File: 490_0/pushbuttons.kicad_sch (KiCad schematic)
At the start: 5 parts, among them SW1 SW_Push0, SW2 SW_Push1, SW3 SW_Push2, SW4 SW_Push3, SW5 SW_Push4

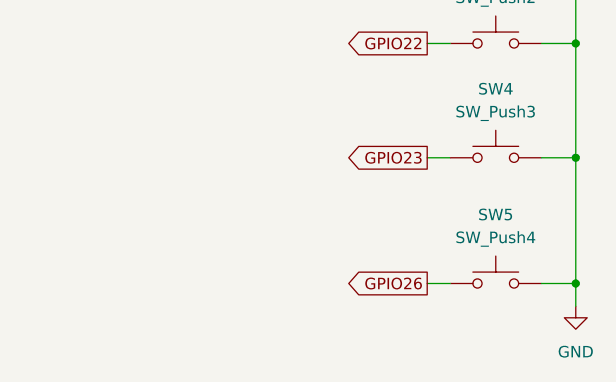
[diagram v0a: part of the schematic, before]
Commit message: US letter format
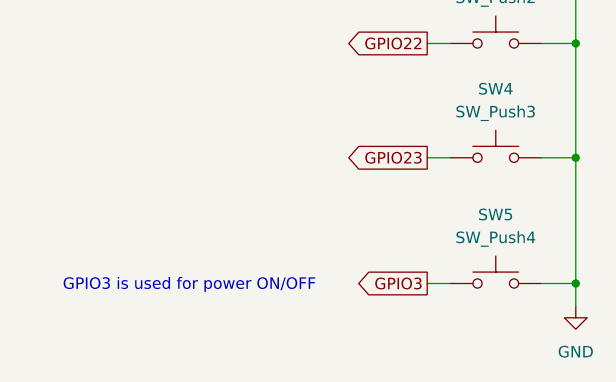
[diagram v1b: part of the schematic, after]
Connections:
- net GPIO26 renamed GPIO3
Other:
- note added: "GPIO3 is used for power ON/OFF"
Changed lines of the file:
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@@
 	(generator "eeschema")
 	(generator_version "9.0")
-	(paper "A4")
+	(paper "USLetter")
+	(text "GPIO3 is used for power ON/OFF\n"
+		(exclude_from_sim no)
+		(at 109.474 114.554 0)
+		(effects
+			(font
+				(size 1.27 1.27)
+			)
+		)
+	)
 	(junction
 		(at 152.4 100.33)
@@
 		)
 	)
-	(global_label "GPIO26"
+	(global_label "GPIO3"
 		(shape output)
 		(at 135.89 114.3 180)
@@
 		)
 		(property "Intersheetrefs" "${INTERSHEET_REFS}"
-			(at 126.0105 114.3 0)
+			(at 127.22 114.3 0)
 			(effects
 				(font

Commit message: Fixed buttons
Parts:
- removed SW1: SW_Push0, symbol Switch:SW_Push
- removed SW2: SW_Push1, symbol Switch:SW_Push
- removed SW3: SW_Push2, symbol Switch:SW_Push
- removed SW4: SW_Push3, symbol Switch:SW_Push
- removed SW5: SW_Push4, symbol Switch:SW_Push
- added R3, R4, R5, R6: 10k, symbol Device:R
- added SW10, SW11, SW12, SW6, SW7: SW_Push0, symbol Switch:SW_Push
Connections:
- net GND: now also SW10.1, SW11.1, SW12.1, SW6.1, SW7.1
- net GPIO16: now also R3.1, SW6.2
- net GPIO17: now also R4.1, SW7.2
- net GPIO22: now also R5.1, SW10.2
- net GPIO23: now also R6.1, SW11.2
- new net +3.3V: R3.2, R4.2, R5.2, R6.2, SW12.2
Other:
- note added: "CM4 has built in internal 1.8kΩ pull up to GPIO_VREF on GPIO3"
- note added: "To Turn ON: When the Pi is OFF/halted - shorting GPIO3 to Ground wakes it up. To Turn OFF: When the Pi is ON - run a script that listens for a button press on GPIO3 and issues the command sudo shutdown -h now"
- note removed: "GPIO3 is used for power ON/OFF"

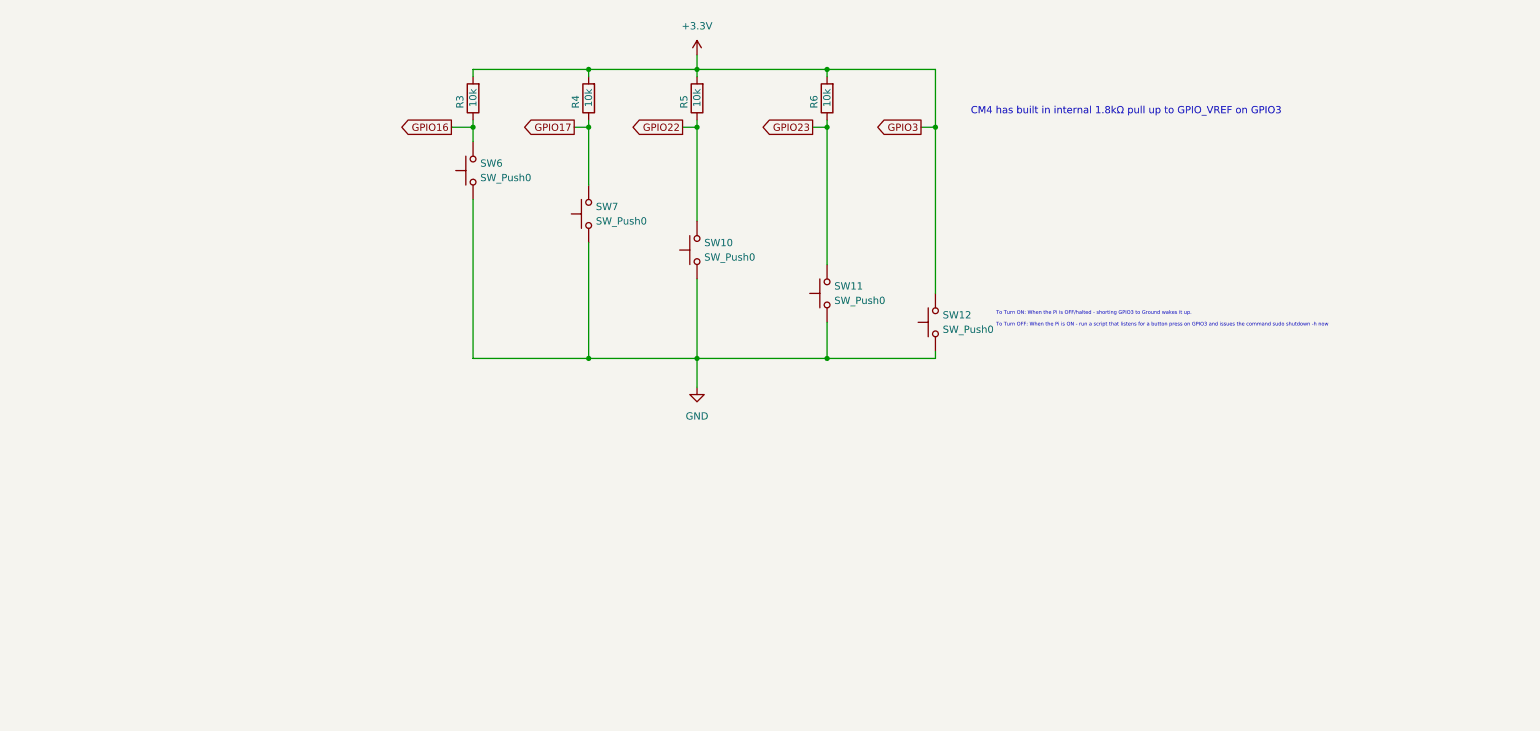
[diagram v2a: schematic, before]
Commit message: Added debouncing to the buttons
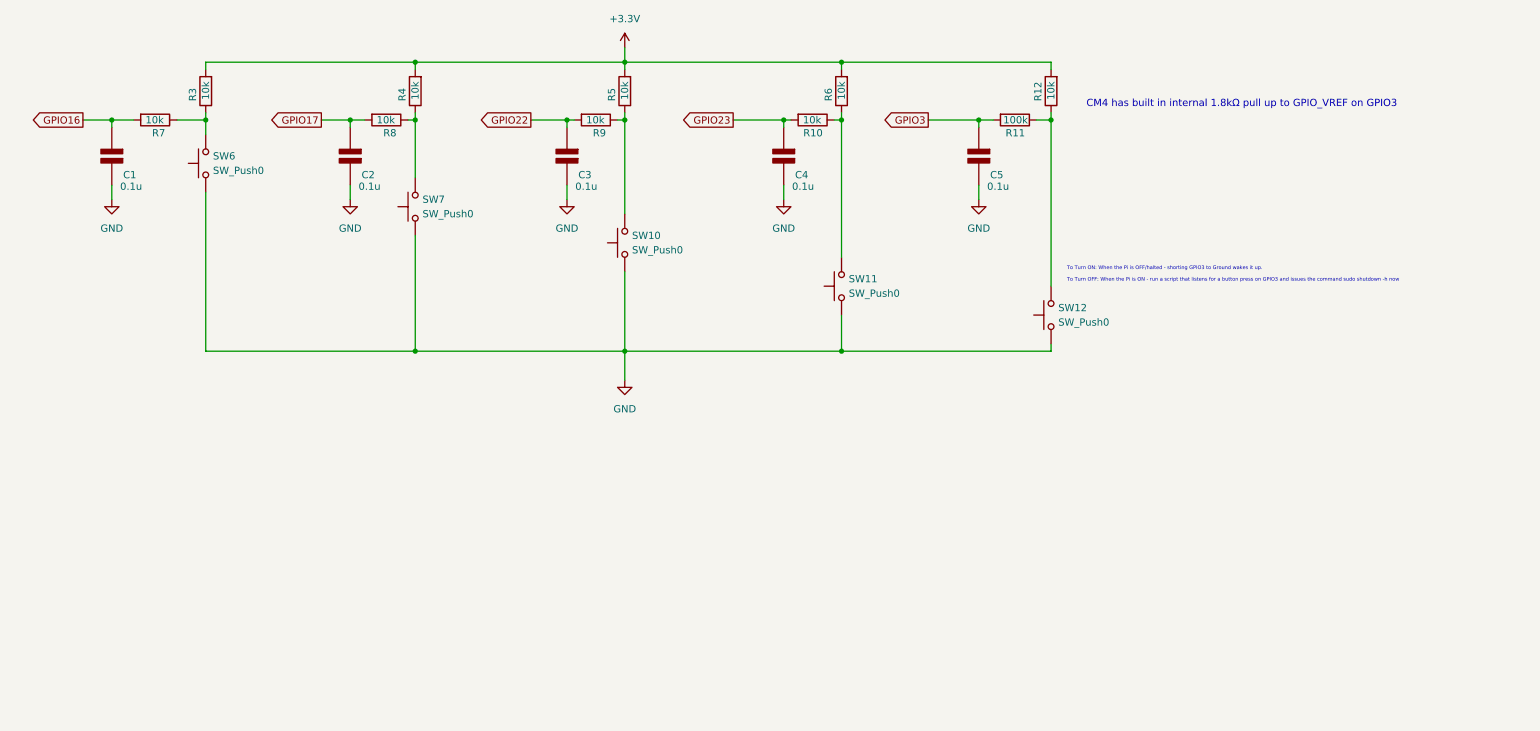
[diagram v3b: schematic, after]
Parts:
- added C1, C2, C3, C4, C5: 0.1u, symbol PCM_Elektuur:C
- added R10, R12, R7, R8, R9: 10k, symbol Device:R
- added R11: 100k, symbol Device:R
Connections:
- net +3.3V: now also R12.2; no longer SW12.2
- net GND: now also C1.2 (-), C2.2 (-), C3.2 (-), C4.2 (-), C5.2 (-)
- net GPIO16: now also C1.1 (+), R7.2; no longer R3.1, SW6.2
- net GPIO17: now also C2.1 (+), R8.2; no longer R4.1, SW7.2
- net GPIO22: now also C3.1 (+), R9.2; no longer R5.1, SW10.2
- net GPIO23: now also C4.1 (+), R10.2; no longer R6.1, SW11.2
- new net: R11.1, R12.1, SW12.2
- new net: R3.1, R7.1, SW6.2
- new net: R5.1, R9.1, SW10.2
- new net: R10.1, R6.1, SW11.2
- new net: R4.1, R8.1, SW7.2
- new net GPIO3: C5.1 (+), R11.2
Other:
- moved on the sheet: R3, R4, R5, R6, SW10, SW11, SW12, SW6, SW7

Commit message: Minor fixes
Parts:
- R11: value 100k -> 10k
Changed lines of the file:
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@@
 			)
 		)
-		(property "Value" "100k"
+		(property "Value" "10k"
 			(at 190.246 62.23 90)
 			(effects

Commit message: Minor updates
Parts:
- renumbered C1 to C51, C2 to C52, C3 to C53, C4 to C54, C5 to C55, R3 to R38, R4 to R39, R5 to R40, R6 to R41, R12 to R42, R7 to R43, R8 to R44, R9 to R45, R10 to R46, R11 to R47, SW6 to SW4, SW7 to SW5, SW10 to SW6, SW11 to SW7, SW12 to SW8

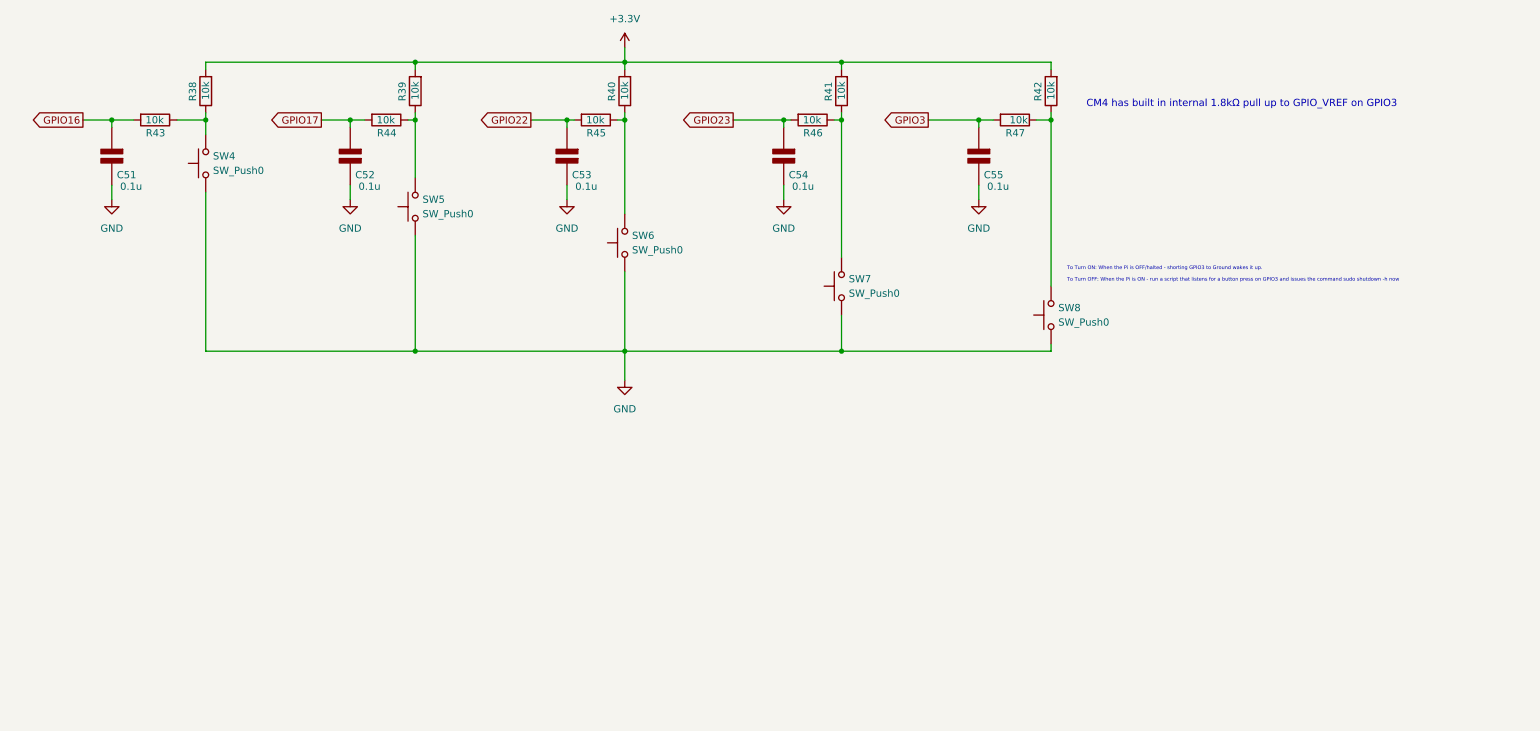
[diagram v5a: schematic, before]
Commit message: Updated box diagram
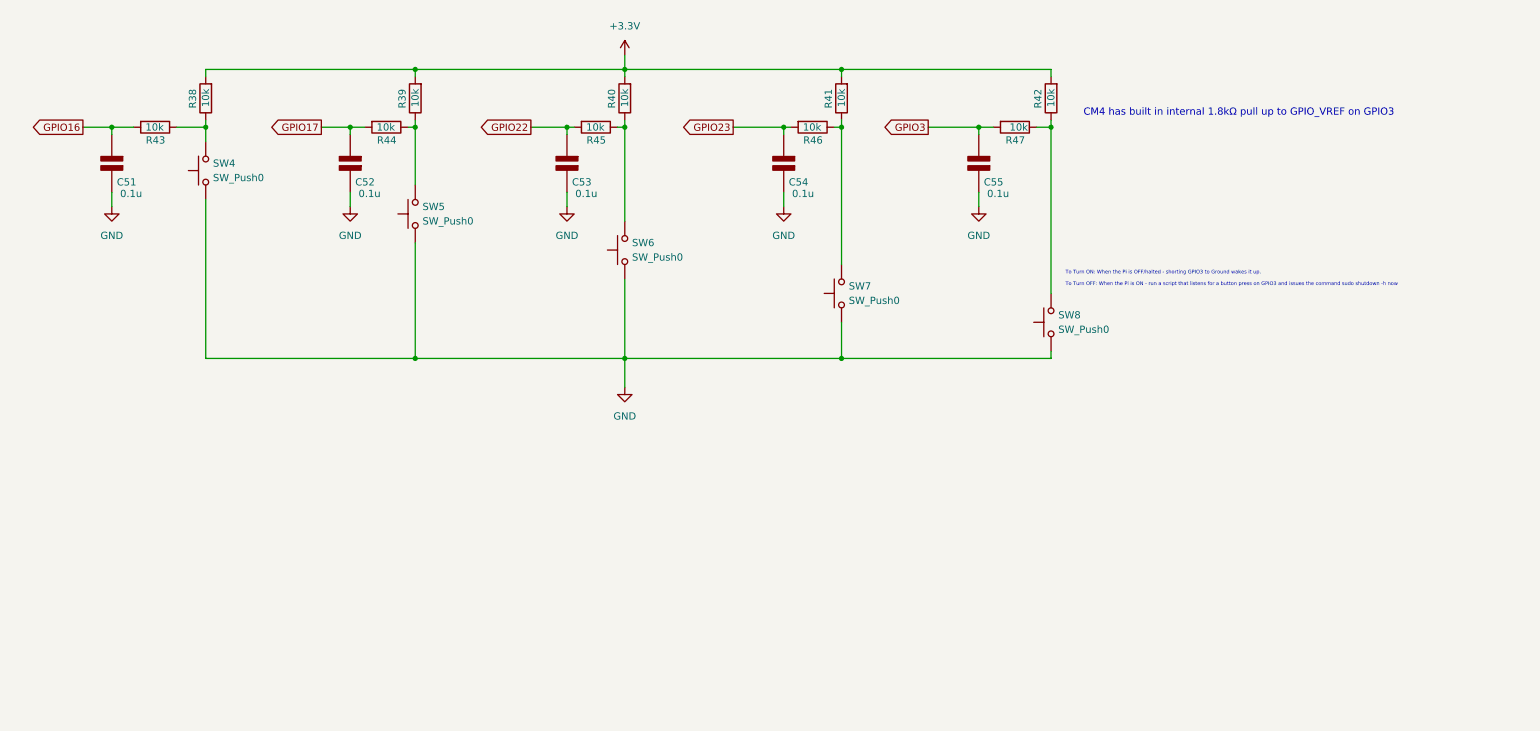
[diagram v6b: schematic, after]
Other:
- moved on the sheet: C51, C52, C53, C54, C55, R38, R39, R40, R41, R42, R43, R44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

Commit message: BOM + ESD replacement for HDMI
Started BOM and changed ESD chips that were obsolete. Also added 2 pin connectors
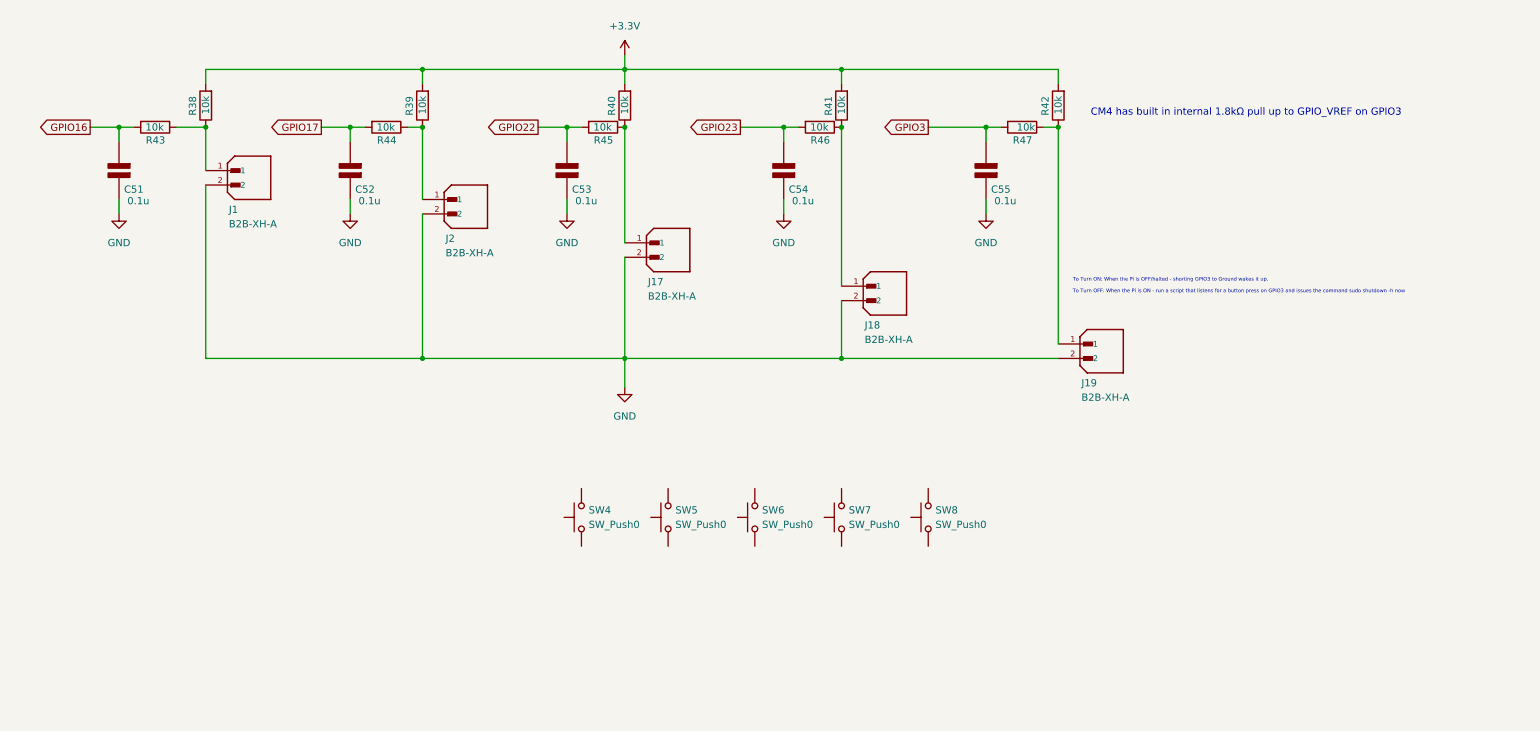
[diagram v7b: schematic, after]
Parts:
- added J1, J17, J18, J19, J2: B2B-XH-A, B2B-XH-A:JST_B2B-XH-A, symbol capstone_parts:B2B-XH-A
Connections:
- net GND: now also J1.2, J17.2, J18.2, J19.2, J2.2; no longer SW4.1, SW5.1, SW6.1, SW7.1, SW8.1
- net at R42.1, R47.1: now also J19.1; no longer SW8.2
- net at R38.1, R43.1: now also J1.1; no longer SW4.2
- net at R40.1, R45.1: now also J17.1; no longer SW6.2
- net at R41.1, R46.1: now also J18.1; no longer SW7.2
- net at R39.1, R44.1: now also J2.1; no longer SW5.2
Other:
- moved on the sheet: C51, C52, C53, C54, C55, R38, R39, R40, R41, R42, R45, R46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

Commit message: Added another button + address fix
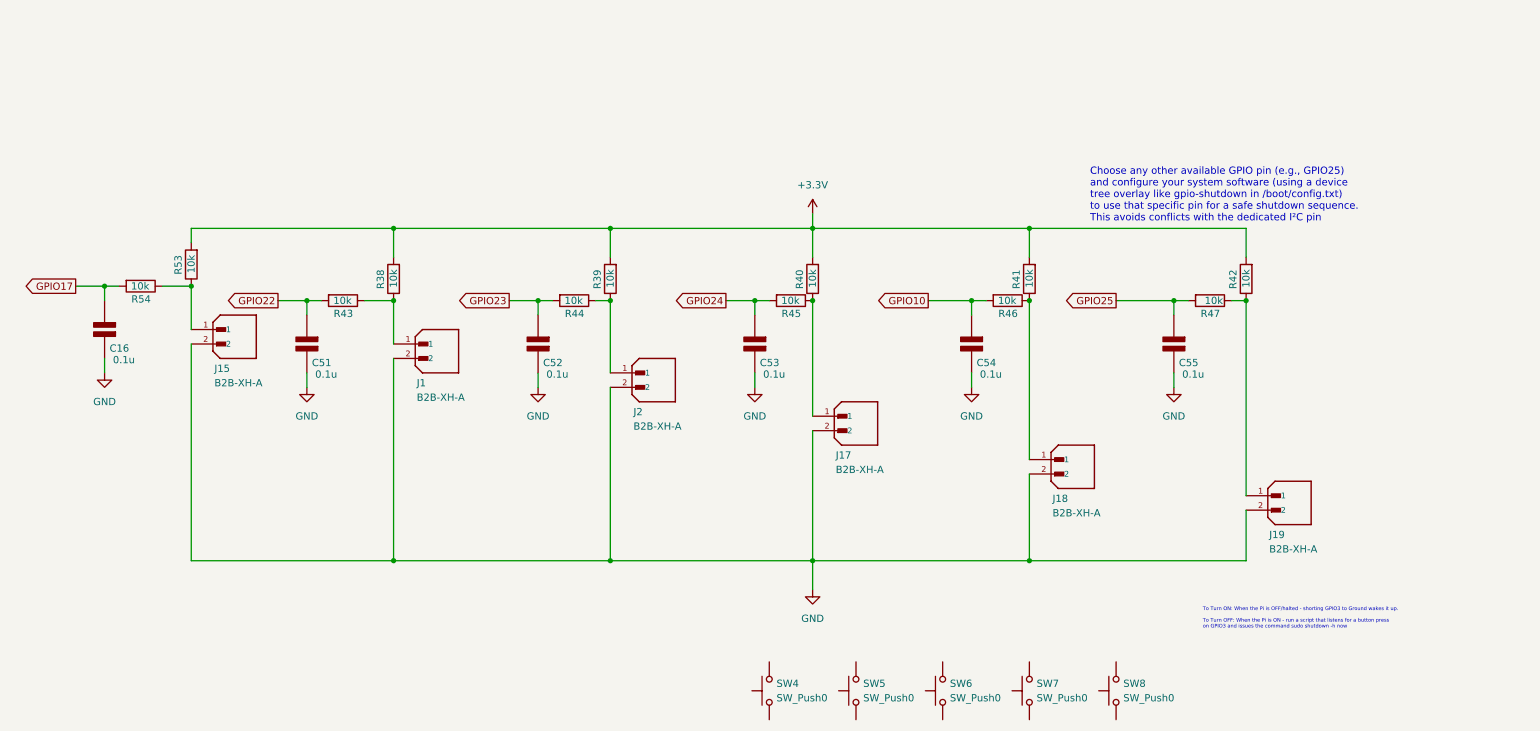
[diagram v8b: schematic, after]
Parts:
- added C16: 0.1u, symbol PCM_Elektuur:C
- added J15: B2B-XH-A, B2B-XH-A:JST_B2B-XH-A, symbol capstone_parts:B2B-XH-A
- added R53, R54: 10k, symbol Device:R
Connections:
- net GPIO16 is gone; now on net GPIO22: C51.1 (+), R43.2
- net +3.3V: now also R53.2
- net GND: now also C16.2 (-), J15.2
- net GPIO17: now also C16.1 (+), R54.2; no longer C52.1 (+), R44.2
- net GPIO22: no longer C53.1 (+), R45.2
- net GPIO23: now also C52.1 (+), R44.2; no longer C54.1 (+), R46.2
- net GPIO3 renamed GPIO25
- new net: J15.1, R53.1, R54.1
- new net GPIO10: C54.1 (+), R46.2
- new net GPIO24: C53.1 (+), R45.2
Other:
- note added: "Choose any other available GPIO pin (e.g., GPIO25) and configure your system software (using a device tree overlay like gpio-shutdown in /boot/config.txt) to use that specific pin for a safe shutdown sequence. This avoids conflicts with the dedicated I²C pin"
- note removed: "CM4 has built in internal 1.8kΩ pull up to GPIO_VREF on GPIO3"
- moved on the sheet: C51, C52, C53, C54, C55, J1, J17, J18, J19, J2, R38, R39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
